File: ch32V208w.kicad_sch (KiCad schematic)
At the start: 26 parts, among them J1 TC2050, J2 Conn_01x02, J3 Conn_01x02, J4 Conn_01x02, U1 CH32V208WBU6, Y1 32MHz, Y2 32768Hz

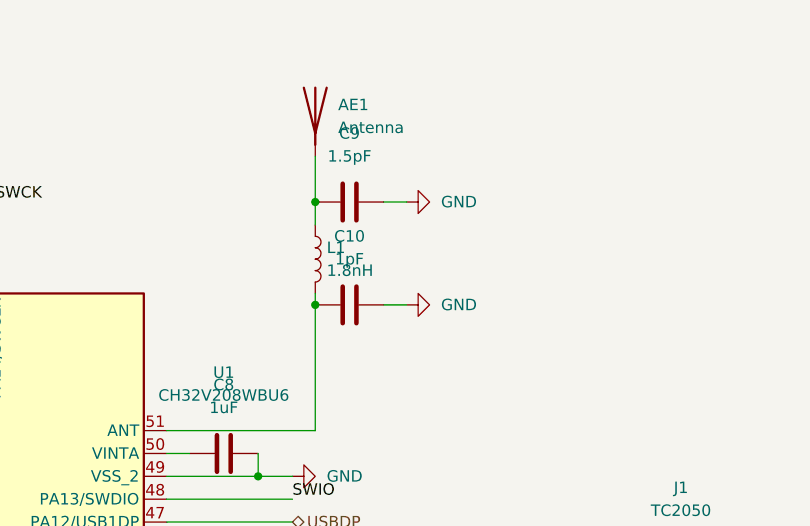
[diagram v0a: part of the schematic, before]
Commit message: Added Antenna design
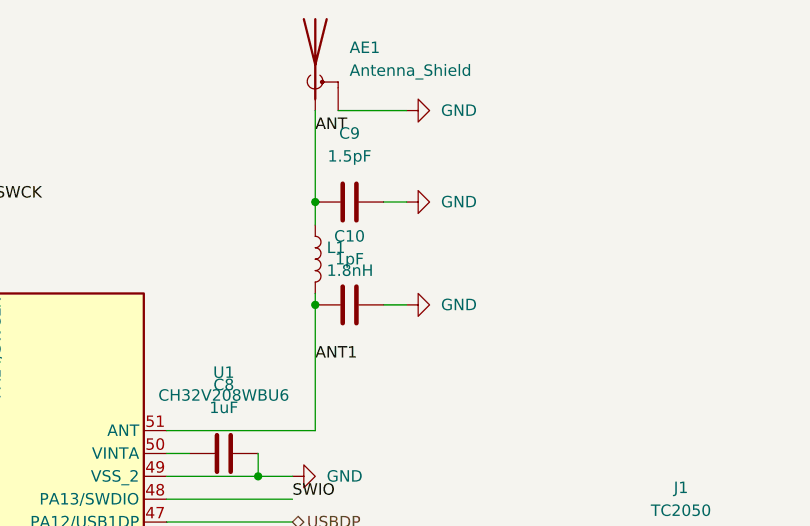
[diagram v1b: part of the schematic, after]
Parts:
- removed AE1: Antenna, wch-antenna-pretty:ANT-F-1-2.4G-1.6MM-FR4-WCH, symbol Device:Antenna
- added AE1: Antenna_Shield, wch-antenna-pretty:ANT-F-1-2.4G-1.6MM-FR4-WCH, symbol Device:Antenna_Shield
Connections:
- net GND: now also AE1.2 (Shield)
- net ANT1: now reaches C10.1, L1.2, U1.51 (ANT)
- net ANT: now reaches C9.1, L1.1
- net ANT: now also AE1.1 (A)
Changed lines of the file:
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@@
     (stroke (width 0) (type default))
   )
-  (wire (pts (xy 187.96 45.72) (xy 187.96 50.8))
+  (wire (pts (xy 187.96 40.64) (xy 187.96 50.8))
     (stroke (width 0) (type default))
   )
@@
     (stroke (width 0) (type default))
   )
+  (wire (pts (xy 190.5 40.64) (xy 198.12 40.64))
+    (stroke (width 0) (type default))
+  )
   (wire (pts (xy 187.96 76.2) (xy 171.45 76.2))
     (stroke (width 0) (type default))
@@
     (effects (font (size 1.27 1.27)) (justify left bottom))
   )
+  (label "ANT1" (at 187.96 68.58 0) (fields_autoplaced)
+    (effects (font (size 1.27 1.27)) (justify left bottom))
+  )
   (label "OSC_OUT" (at 43.18 96.52 0) (fields_autoplaced)
     (effects (font (size 1.27 1.27)) (justify left bottom))
@@
   )
   (label "TXD" (at 242.57 88.9 0) (fields_autoplaced)
+    (effects (font (size 1.27 1.27)) (justify left bottom))
+  )
+  (label "ANT" (at 187.96 43.18 0) (fields_autoplaced)
     (effects (font (size 1.27 1.27)) (justify left bottom))
   )
@@
     )
   )
+  (symbol (lib_id "Device:Antenna_Shield") (at 187.96 35.56 0) (unit 1)
+    (in_bom yes) (on_board yes) (dnp no) (fields_autoplaced)
+    (property "Reference" "AE1" (at 191.77 33.655 0)
+      (effects (font (size 1.27 1.27)) (justify left))
+    )
+    (property "Value" "Antenna_Shield" (at 191.77 36.195 0)
+      (effects (font (size 1.27 1.27)) (justify left))
+    )
+    (property "Footprint" "wch-antenna-pretty:ANT-F-1-2.4G-1.6MM-FR4-WCH" (at 187.96 33.02 0)
+      (effects (font (size 1.27 1.27)) hide)
+    )
+    (property "Datasheet" "~" (at 187.96 33.02 0)
+      (effects (font (size 1.27 1.27)) hide)
+    )
+    (pin "1")
+    (pin "2")
+    (instances
+      (project "reaction-trainer"
+        (path "/726cb70d-0185-4970-973b-037545fc3942/f1bd1f0b-9f19-4bc6-92d8-e7cd49ef503b"
+          (reference "AE1") (unit 1)
+        )
+      )
+    )
+  )
   (symbol (lib_id "Device:C") (at 80.01 76.2 90) (unit 1)
     (in_bom yes) (on_board yes) (dnp no) (fields_autoplaced)
@@
     )
   )
-  (symbol (lib_id "Device:Antenna") (at 187.96 40.64 0) (unit 1)
-    (in_bom yes) (on_board yes) (dnp no) (fields_autoplaced)
-    (property "Reference" "AE1" (at 190.5 40.005 0)
-      (effects (font (size 1.27 1.27)) (justify left))
-    )
-    (property "Value" "Antenna" (at 190.5 42.545 0)
-      (effects (font (size 1.27 1.27)) (justify left))
-    )
-    (property "Footprint" "wch-antenna-pretty:ANT-F-1-2.4G-1.6MM-FR4-WCH" (at 187.96 40.64 0)
-      (effects (font (size 1.27 1.27)) hide)
-    )
-    (property "Datasheet" "~" (at 187.96 40.64 0)
-      (effects (font (size 1.27 1.27)) hide)
-    )
-    (pin "1")
-    (instances
-      (project "reaction-trainer"
-        (path "/726cb70d-0185-4970-973b-037545fc3942/f1bd1f0b-9f19-4bc6-92d8-e7cd49ef503b"
-          (reference "AE1") (unit 1)
-        )
-      )
-    )
-  )
   (symbol (lib_id "power:GND") (at 242.57 96.52 90) (unit 1)
     (in_bom yes) (on_board yes) (dnp no) (fields_autoplaced)
@@
         )
       )
+    )
+  )
+  (symbol (lib_id "power:GND") (at 198.12 40.64 90) (unit 1)
+    (in_bom yes) (on_board yes) (dnp no) (fields_autoplaced)
+    (property "Reference" "#PWR067" (at 204.47 40.64 0)
+      (effects (font (size 1.27 1.27)) hide)
+    )
+    (property "Value" "GND" (at 201.93 40.64 90)
+      (effects (font (size 1.27 1.27)) (justify right))
+    )
+    (property "Footprint" "" (at 198.12 40.64 0)
+      (effects (font (size 1.27 1.27)) hide)
+    )
+    (property "Datasheet" "" (at 198.12 40.64 0)
+      (effects (font (size 1.27 1.27)) hide)
+    )
+    (pin "1")
+    (instances
+      (project "reaction-trainer"
+        (path "/726cb70d-0185-4970-973b-037545fc3942/f1bd1f0b-9f19-4bc6-92d8-e7cd49ef503b"
+          (reference "#PWR067") (unit 1)
+        )
+      )

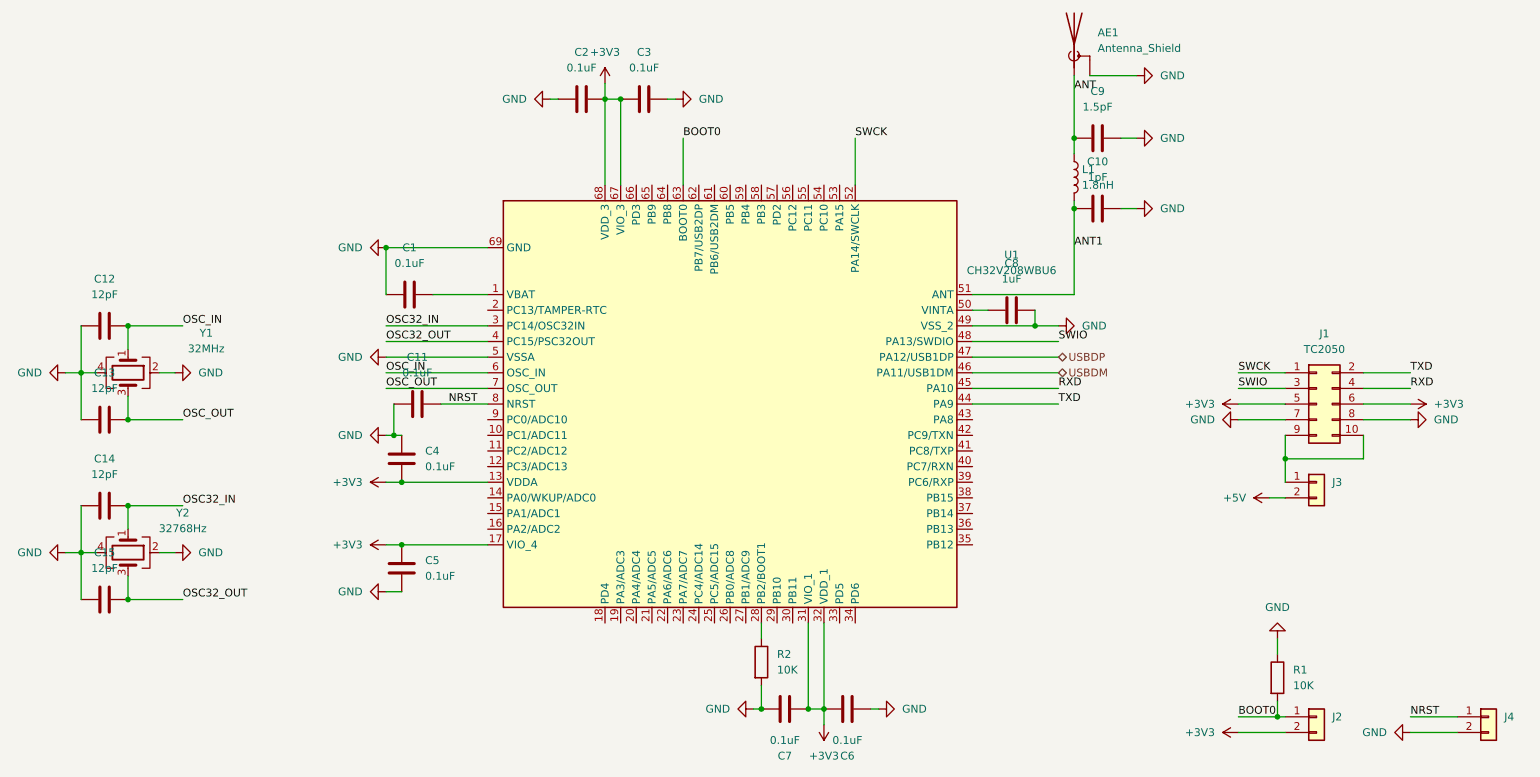
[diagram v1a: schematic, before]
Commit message: Removed audio, more routing
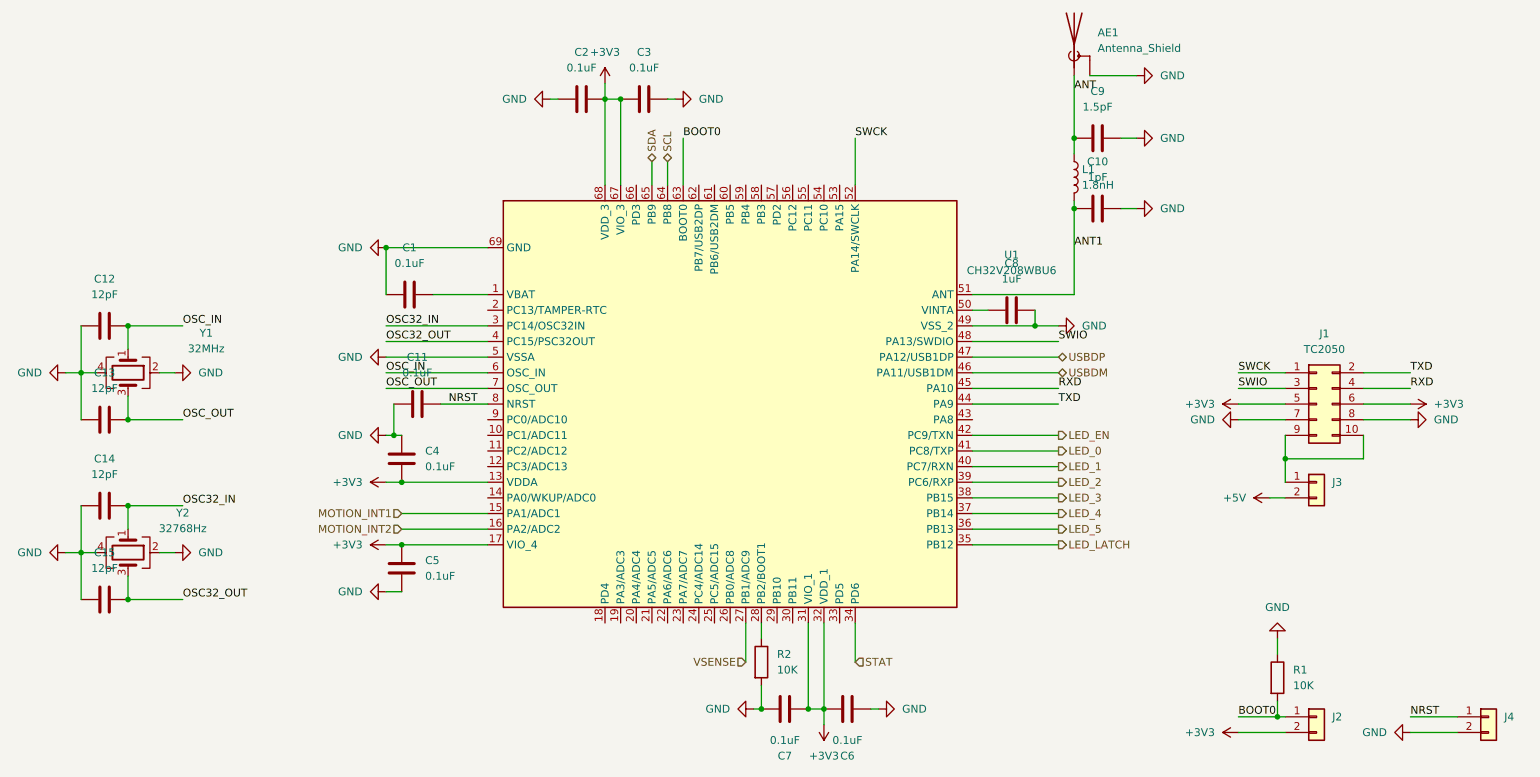
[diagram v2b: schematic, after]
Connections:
- net MOTION_INT1: now reaches U1.15 (PA1/ADC1)
- net MOTION_INT2: now reaches U1.16 (PA2/ADC2)
- net VSENSE: now reaches U1.27 (PB1/ADC9)
- net STAT: now reaches U1.34 (PD6)
- net LED_LATCH: now reaches U1.35 (PB12)
- net LED_5: now reaches U1.36 (PB13)
- net LED_4: now reaches U1.37 (PB14)
- net LED_3: now reaches U1.38 (PB15)
- net LED_2: now reaches U1.39 (PC6/RXP)
- net LED_1: now reaches U1.40 (PC7/RXN)
- net LED_0: now reaches U1.41 (PC8/TXP)
- net LED_EN: now reaches U1.42 (PC9/TXN)
- net SCL: now reaches U1.64 (PB8)
- net SDA: now reaches U1.65 (PB9)
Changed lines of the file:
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@@
+    (stroke (width 0) (type default))
+  )
+  (wire (pts (xy 119.38 54.61) (xy 119.38 58.42))
     (stroke (width 0) (type default))
   )
@@
     (stroke (width 0) (type default))
   )
+  (wire (pts (xy 121.92 54.61) (xy 121.92 58.42))
+    (stroke (width 0) (type default))
+  )
   (wire (pts (xy 222.25 102.87) (xy 234.95 102.87))
     (stroke (width 0) (type default))
@@
     (stroke (width 0) (type default))
   )
+  (wire (pts (xy 171.45 116.84) (xy 185.42 116.84))
+    (stroke (width 0) (type default))
+  )
   (wire (pts (xy 111.76 41.91) (xy 111.76 44.45))
     (stroke (width 0) (type default))
@@
     (stroke (width 0) (type default))
   )
+  (wire (pts (xy 171.45 99.06) (xy 185.42 99.06))
+    (stroke (width 0) (type default))
+  )
   (wire (pts (xy 137.16 143.51) (xy 135.89 143.51))
     (stroke (width 0) (type default))
@@
     (stroke (width 0) (type default))
   )
+  (wire (pts (xy 171.45 114.3) (xy 185.42 114.3))
+    (stroke (width 0) (type default))
+  )
   (wire (pts (xy 242.57 144.78) (xy 250.19 144.78))
     (stroke (width 0) (type default))
@@
     (stroke (width 0) (type default))
   )
+  (wire (pts (xy 171.45 106.68) (xy 185.42 106.68))
+    (stroke (width 0) (type default))
+  )
   (wire (pts (xy 171.45 86.36) (xy 185.42 86.36))
     (stroke (width 0) (type default))
@@
     (stroke (width 0) (type default))
   )
+  (wire (pts (xy 78.74 114.3) (xy 92.71 114.3))
+    (stroke (width 0) (type default))
+  )
   (wire (pts (xy 34.29 125.73) (xy 43.18 125.73))
     (stroke (width 0) (type default))
@@
     (stroke (width 0) (type default))
   )
+  (wire (pts (xy 78.74 111.76) (xy 92.71 111.76))
+    (stroke (width 0) (type default))
+  )
   (wire (pts (xy 220.98 142.24) (xy 220.98 144.78))
     (stroke (width 0) (type default))
@@
     (stroke (width 0) (type default))
   )
+  (wire (pts (xy 171.45 104.14) (xy 185.42 104.14))
+    (stroke (width 0) (type default))
+  )
   (wire (pts (xy 85.09 93.98) (xy 92.71 93.98))
     (stroke (width 0) (type default))
@@
     (stroke (width 0) (type default))
   )
+  (wire (pts (xy 171.45 111.76) (xy 185.42 111.76))
+    (stroke (width 0) (type default))
+  )
   (wire (pts (xy 222.25 99.06) (xy 222.25 102.87))
     (stroke (width 0) (type default))
   )
+  (wire (pts (xy 134.62 129.54) (xy 134.62 135.89))
+    (stroke (width 0) (type default))
+  )
   (wire (pts (xy 137.16 129.54) (xy 137.16 132.08))
     (stroke (width 0) (type default))
@@
     (stroke (width 0) (type default))
   )
+  (wire (pts (xy 152.4 129.54) (xy 152.4 135.89))
+    (stroke (width 0) (type default))
+  )
   (wire (pts (xy 190.5 40.64) (xy 198.12 40.64))
     (stroke (width 0) (type default))
@@
     (stroke (width 0) (type default))
   )
+  (wire (pts (xy 171.45 101.6) (xy 185.42 101.6))
+    (stroke (width 0) (type default))
+  )
   (wire (pts (xy 34.29 110.49) (xy 43.18 110.49))
     (stroke (width 0) (type default))
@@
     (stroke (width 0) (type default))
   )
+  (wire (pts (xy 171.45 109.22) (xy 185.42 109.22))
+    (stroke (width 0) (type default))
+  )
   (wire (pts (xy 144.78 129.54) (xy 144.78 143.51))
     (stroke (width 0) (type default))
@@
     (effects (font (size 1.27 1.27)) (justify left bottom))
   )
+  (hierarchical_label "SDA" (shape bidirectional) (at 119.38 54.61 90) (fields_autoplaced)
+    (effects (font (size 1.27 1.27)) (justify left))
+  )
+  (hierarchical_label "LED_LATCH" (shape output) (at 185.42 116.84 0) (fields_autoplaced)
+    (effects (font (size 1.27 1.27)) (justify left))
+  )
+  (hierarchical_label "MOTION_INT1" (shape input) (at 78.74 111.76 180) (fields_autoplaced)
+    (effects (font (size 1.27 1.27)) (justify right))
+  )
+  (hierarchical_label "SCL" (shape bidirectional) (at 121.92 54.61 90) (fields_autoplaced)
+    (effects (font (size 1.27 1.27)) (justify left))
+  )
+  (hierarchical_label "LED_4" (shape output) (at 185.42 111.76 0) (fields_autoplaced)
+    (effects (font (size 1.27 1.27)) (justify left))
+  )
+  (hierarchical_label "LED_2" (shape output) (at 185.42 106.68 0) (fields_autoplaced)
+    (effects (font (size 1.27 1.27)) (justify left))
+  )
+  (hierarchical_label "MOTION_INT2" (shape input) (at 78.74 114.3 180) (fields_autoplaced)
+    (effects (font (size 1.27 1.27)) (justify right))
+  )
+  (hierarchical_label "LED_1" (shape output) (at 185.42 104.14 0) (fields_autoplaced)
+    (effects (font (size 1.27 1.27)) (justify left))
+  )
+  (hierarchical_label "VSENSE" (shape input) (at 134.62 135.89 180) (fields_autoplaced)
+    (effects (font (size 1.27 1.27)) (justify right))
+  )
   (hierarchical_label "USBDM" (shape bidirectional) (at 185.42 88.9 0) (fields_autoplaced)
     (effects (font (size 1.27 1.27)) (justify left))
   )
+  (hierarchical_label "LED_5" (shape output) (at 185.42 114.3 0) (fields_autoplaced)
+    (effects (font (size 1.27 1.27)) (justify left))
+  )
+  (hierarchical_label "LED_0" (shape output) (at 185.42 101.6 0) (fields_autoplaced)
+    (effects (font (size 1.27 1.27)) (justify left))
+  )
+  (hierarchical_label "LED_EN" (shape output) (at 185.42 99.06 0) (fields_autoplaced)
+    (effects (font (size 1.27 1.27)) (justify left))
+  )
   (hierarchical_label "USBDP" (shape bidirectional) (at 185.42 86.36 0) (fields_autoplaced)
     (effects (font (size 1.27 1.27)) (justify left))
   )
+  (hierarchical_label "LED_3" (shape output) (at 185.42 109.22 0) (fields_autoplaced)
+    (effects (font (size 1.27 1.27)) (justify left))
+  )
+  (hierarchical_label "STAT" (shape input) (at 152.4 135.89 0) (fields_autoplaced)
+    (effects (font (size 1.27 1.27)) (justify left))
+  )

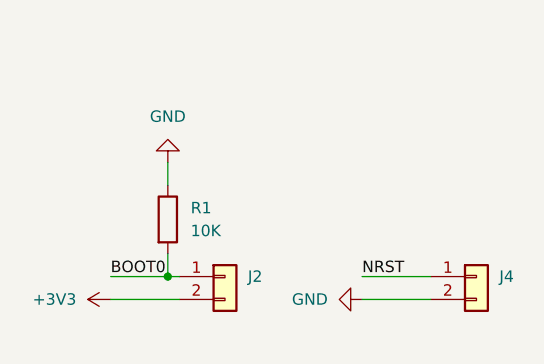
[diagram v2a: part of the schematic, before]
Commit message: Added JLPCB DRCs, antenna hatching
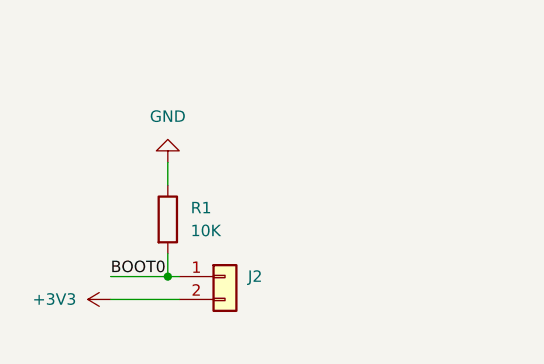
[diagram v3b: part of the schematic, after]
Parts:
- removed J4: Conn_01x02, Connector_PinHeader_2.54mm:PinHeader_1x02_P2.54mm_Vertical, symbol Connector_Generic:Conn_01x02
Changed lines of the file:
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@@
-    (stroke (width 0) (type default))
-  )
-  (wire (pts (xy 242.57 144.78) (xy 250.19 144.78))
     (stroke (width 0) (type default))
   )
@@
     (stroke (width 0) (type default))
   )
-  (wire (pts (xy 242.57 147.32) (xy 250.19 147.32))
-    (stroke (width 0) (type default))
-  )
   (wire (pts (xy 187.96 50.8) (xy 187.96 53.34))
     (stroke (width 0) (type default))
@@
   )
   (label "BOOT0" (at 214.63 144.78 0) (fields_autoplaced)
-    (effects (font (size 1.27 1.27)) (justify left bottom))
-  )
-  (label "NRST" (at 242.57 144.78 0) (fields_autoplaced)
     (effects (font (size 1.27 1.27)) (justify left bottom))
   )
@@
         (path "/726cb70d-0185-4970-973b-037545fc3942/f1bd1f0b-9f19-4bc6-92d8-e7cd49ef503b"
           (reference "#PWR03") (unit 1)
-        )
-      )
-    )
-  )
-  (symbol (lib_id "power:GND") (at 242.57 147.32 270) (unit 1)
-    (in_bom yes) (on_board yes) (dnp no) (fields_autoplaced)
-    (property "Reference" "#PWR024" (at 236.22 147.32 0)
-      (effects (font (size 1.27 1.27)) hide)
-    )
-    (property "Value" "GND" (at 238.76 147.32 90)
-      (effects (font (size 1.27 1.27)) (justify right))
-    )
-    (property "Footprint" "" (at 242.57 147.32 0)
-      (effects (font (size 1.27 1.27)) hide)
-    )
-    (property "Datasheet" "" (at 242.57 147.32 0)
-      (effects (font (size 1.27 1.27)) hide)
-    )
-    (pin "1")
-    (instances
-      (project "reaction-trainer"
-        (path "/726cb70d-0185-4970-973b-037545fc3942/f1bd1f0b-9f19-4bc6-92d8-e7cd49ef503b"
-          (reference "#PWR024") (unit 1)
         )
       )
@@
         )
       )
-    )
-  )
-  (symbol (lib_id "Connector_Generic:Conn_01x02") (at 255.27 144.78 0) (unit 1)
-    (in_bom yes) (on_board yes) (dnp no) (fields_autoplaced)
-    (property "Reference" "J4" (at 257.81 144.78 0)
-      (effects (font (size 1.27 1.27)) (justify left))
-    )
-    (property "Value" "Conn_01x02" (at 257.81 147.32 0)
-      (effects (font (size 1.27 1.27)) (justify left) hide)
-    )
-    (property "Footprint" "Connector_PinHeader_2.54mm:PinHeader_1x02_P2.54mm_Vertical" (at 255.27 144.78 0)
-      (effects (font (size 1.27 1.27)) hide)
-    )
-    (property "Datasheet" "~" (at 255.27 144.78 0)
-      (effects (font (size 1.27 1.27)) hide)
-    )
-    (pin "1")
-    (pin "2")
-    (instances
-      (project "reaction-trainer"
-        (path "/726cb70d-0185-4970-973b-037545fc3942/f1bd1f0b-9f19-4bc6-92d8-e7cd49ef503b"
-          (reference "J4") (unit 1)
-        )
-      )

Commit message: Field updates, generating fab files
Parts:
- C1, C11, C2, C3, C4, C5, C6, C7: value 0.1uF -> 0.1uF 20%; JLCPCB Part # (none) -> C359190
- C10: value 1pF -> 1pF 5%; JLCPCB Part # (none) -> C307340
- C12, C13: value 12pF -> 12pF 5%; JLCPCB Part # (none) -> C472446
- C14, C15: value 12pF -> 15pF 5%; JLCPCB Part # (none) -> C86285
- C8: value 1uF -> 10uF 20%; JLCPCB Part # (none) -> C315248
- C9: value 1.5pF -> 1.5pF 5%; JLCPCB Part # (none) -> C170150
- J2, J3: value Conn_01x02 -> DNP
- L1: JLCPCB Part # (none) -> C87530
- R1, R2: value 10K -> 10K 5%; JLCPCB Part # (none) -> C2906885
- U1: JLCPCB Part # (none) -> C5187528
- Y1: JLCPCB Part # (none) -> C9009
- Y2: JLCPCB Part # (none) -> C725996
